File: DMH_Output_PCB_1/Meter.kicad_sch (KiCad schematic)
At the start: 63 parts, among them Q1 BC558, Q2 BC558, U1 TL072, U2 LM339, U3 LM339, U4 LM339, U5 LM339, U6 LM339

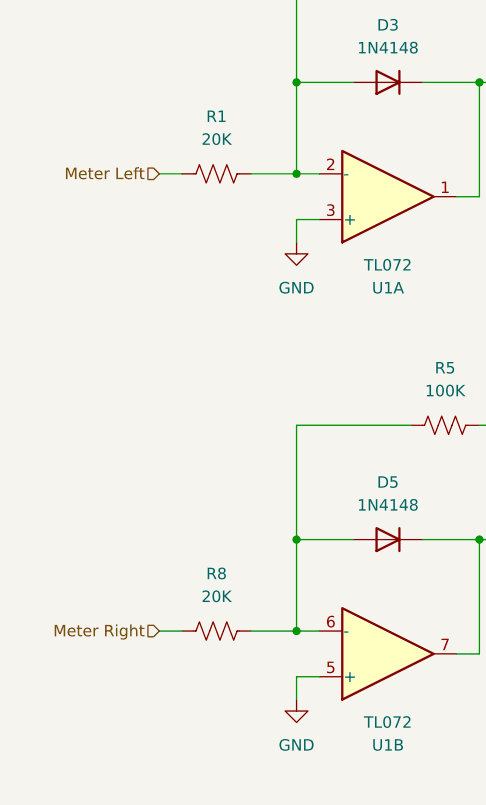
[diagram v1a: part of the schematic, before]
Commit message: Designed preamp circuit
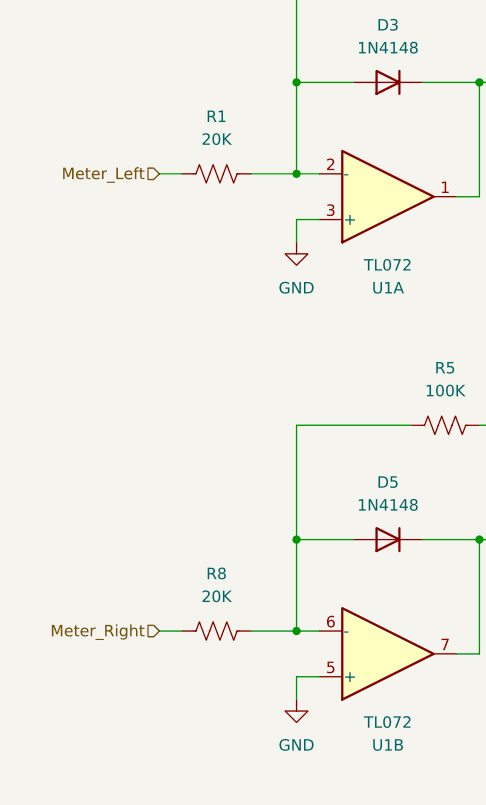
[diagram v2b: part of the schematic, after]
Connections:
- net Meter Left renamed Meter_Left
- net Meter Right renamed Meter_Right
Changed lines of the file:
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@@
 		)
 	)
-	(hierarchical_label "Meter Left"
+	(hierarchical_label "Meter_Left"
 		(shape input)
 		(at 25.4 48.26 180)
@@
 		)
 	)
-	(hierarchical_label "Meter Right"
+	(hierarchical_label "Meter_Right"
 		(shape input)
 		(at 25.4 99.06 180)
